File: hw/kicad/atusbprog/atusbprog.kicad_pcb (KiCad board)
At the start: 2 copper layers, 26 parts, among them J1 SMH-110-02-L-D, J2 Conn_01x04, J3 Conn_01x08, J4 Conn_01x08, J5 Conn_01x08, SW1 SW_Push, SW2 SW_Push, U1 SN74HCT125, U2 AT89S52-24PU, Y1 24 MHz

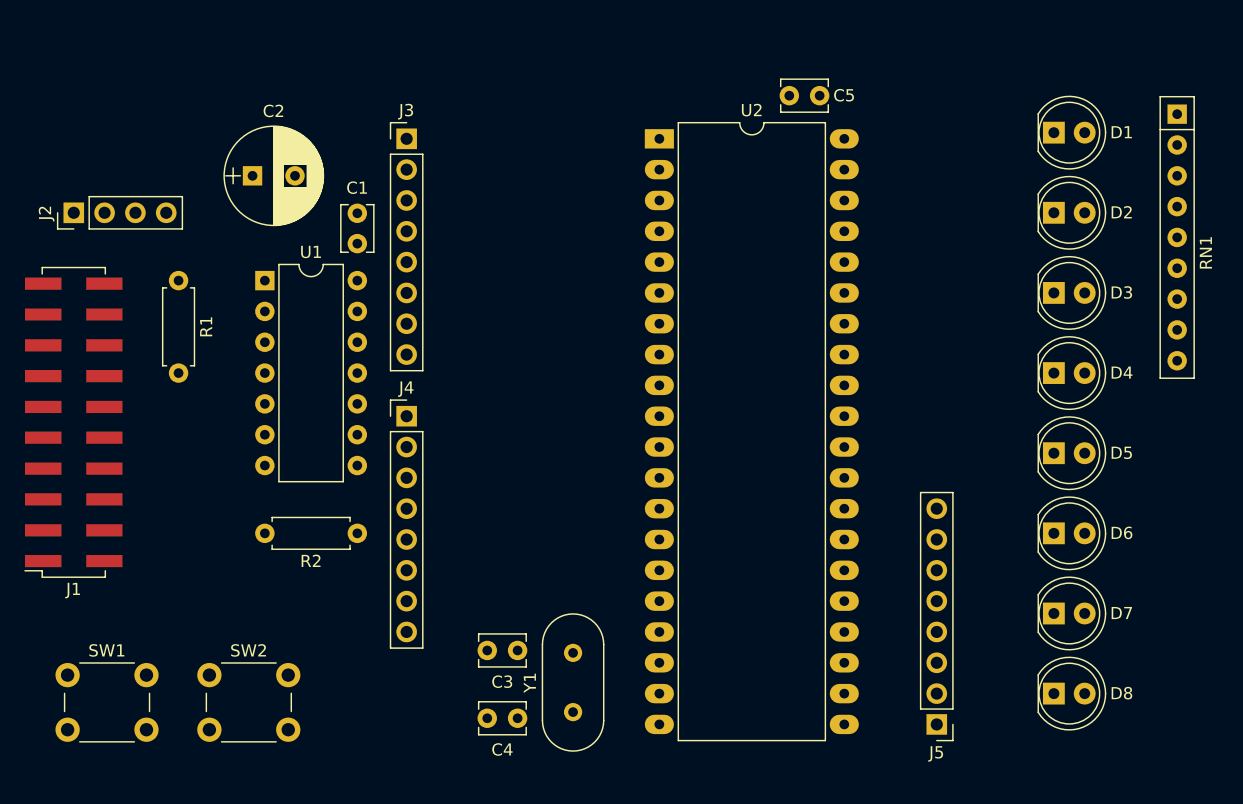
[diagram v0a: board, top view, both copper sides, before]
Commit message: Update to KiCAD 5.1.5, add silk marks
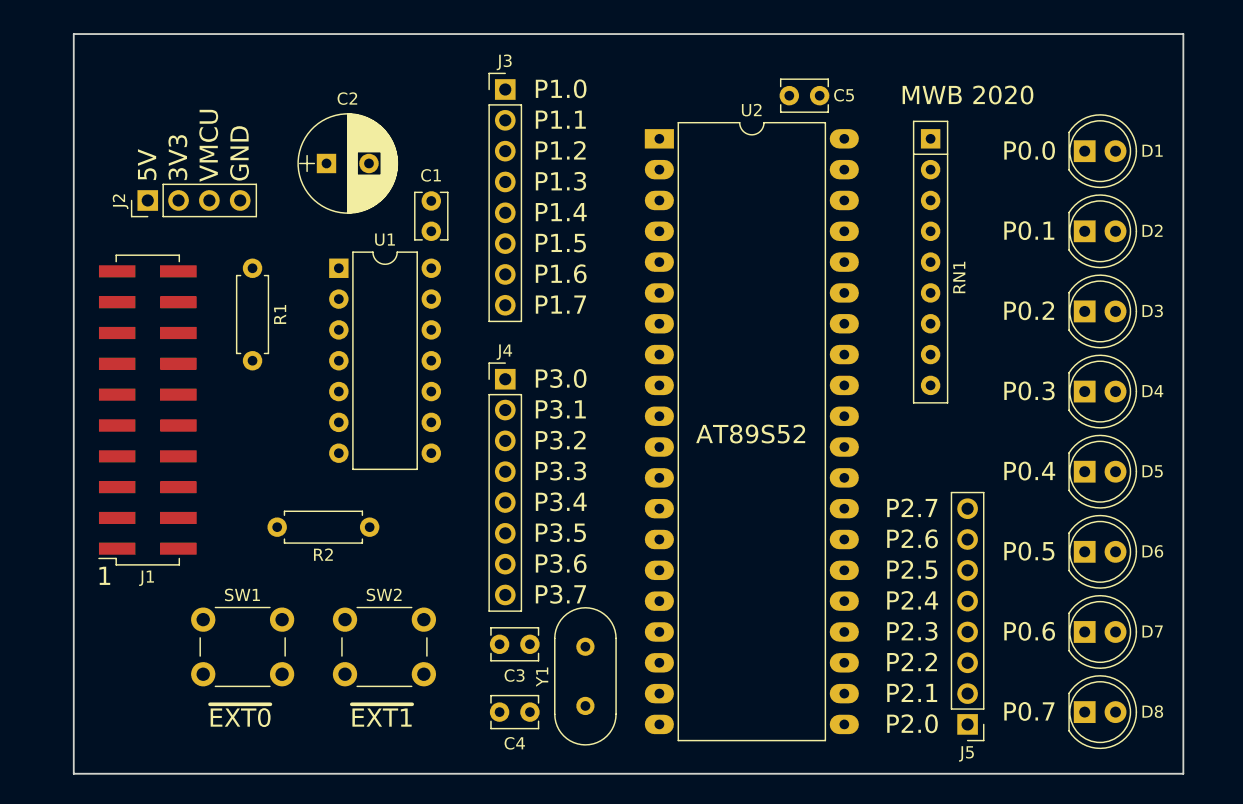
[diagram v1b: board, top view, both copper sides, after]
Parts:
- moved RN1 20.4 mm to (175.3, 74.7)
- moved SW1 12.1 mm to (115.3, 114.3)
- moved SW2 12.1 mm to (127.0, 114.3)
- moved J3 9.09 mm to (140.2, 70.6)
- moved J4 8.68 mm to (140.2, 94.5)
- moved C2 6.18 mm to (125.5, 76.7)
- moved J2 6.18 mm to (110.7, 79.8)
- moved U1 6.18 mm to (126.5, 85.3)
- moved C1 6.18 mm to (134.1, 82.3)
- moved J1 6.18 mm to (110.7, 97.0)
- moved R1 6.18 mm to (119.4, 85.3)
- moved D2 2.96 mm to (188.0, 82.3)
- moved D3 2.96 mm to (188.0, 88.9)
- moved D4 2.96 mm to (188.0, 95.5)
- moved D5 2.96 mm to (188.0, 102.1)
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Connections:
- J1 pad 2: +3V3 -> +VMCU
- J2 pad 3: +3V3 -> +VMCU
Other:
- board outline added: 91.4 x 61 mm
- board text added: "1"
- board text added: "3V3"
- board text added: "5V"
- board text added: "AT89S52"
- board text added: "ATUSBPROG V1"
- board text added: "GND"
- board text added: "MWB 2020"
- board text added: "P0.0"
- board text added: "P0.1"
- board text added: "P0.2"
- board text added: "P0.3"
- board text added: "P0.4"
- board text added: "P0.5"
- board text added: "P0.6"
- board text added: "P0.7"
- board text added: "P1.0"
- board text added: "P1.1"
- board text added: "P1.2"
- board text added: "P1.3"
- board text added: "P1.4"
- board text added: "P1.5"
- board text added: "P1.6"
- board text added: "P1.7"
- board text added: "P2.0"
- board text added: "P2.1"
- board text added: "P2.2"
- board text added: "P2.3"
- board text added: "P2.4"
- board text added: "P2.5"
- board text added: "P2.6"
- board text added: "P2.7"
- board text added: "P3.0"
- board text added: "P3.1"
- board text added: "P3.2"
- board text added: "P3.3"
- board text added: "P3.4"
- board text added: "P3.5"
- board text added: "P3.6"
- board text added: "P3.7"
- board text added: "VMCU"
- board text added: "~EXT0"
- board text added: "~EXT1"

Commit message: Update PCB V1
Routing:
- net /BTN0: track 0.00 -> 52.6 mm
- net ATS_MISO: track 0.00 -> 48.5 mm, vias 0 -> 1
- net EFM_OE_N: track 0.00 -> 43.6 mm
- net /BTN1: track 0.00 -> 39.9 mm
- net Net-(D8-Pad1): track 0.00 -> 36.8 mm
- net ATS_SCK: track 0.00 -> 33.7 mm
- net +VMCU: track 0.00 -> 33.5 mm, vias 0 -> 1
- net ATS_MOSI: track 0.00 -> 33.5 mm
- net Net-(D8-Pad2): track 0.00 -> 33.2 mm
- net EFM_MOSI: track 0.00 -> 32.0 mm, vias 0 -> 1
- net Net-(D7-Pad1): track 0.00 -> 31.3 mm
- net EFM_AUX: track 0.00 -> 30.2 mm, vias 0 -> 2
- net EFM_RST: track 0.00 -> 29.4 mm
- net Net-(D7-Pad2): track 0.00 -> 29.2 mm
- net Net-(D6-Pad1): track 0.00 -> 27.7 mm
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- added copper zone on B.Cu, net +5V
- added copper zone on F.Cu, net GND
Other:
- net class Default: clearance 0.2 -> 0.1524
- rule pad_to_mask_clearance: 0.2 -> 0.0508
- rule trace_clearance: 0.2 -> 0.1524
- rule trace_min: 0.2 -> 0.1524
- rule via_min_drill: 0.3 -> 0.254
- rule via_min_size: 0.4 -> 0.254

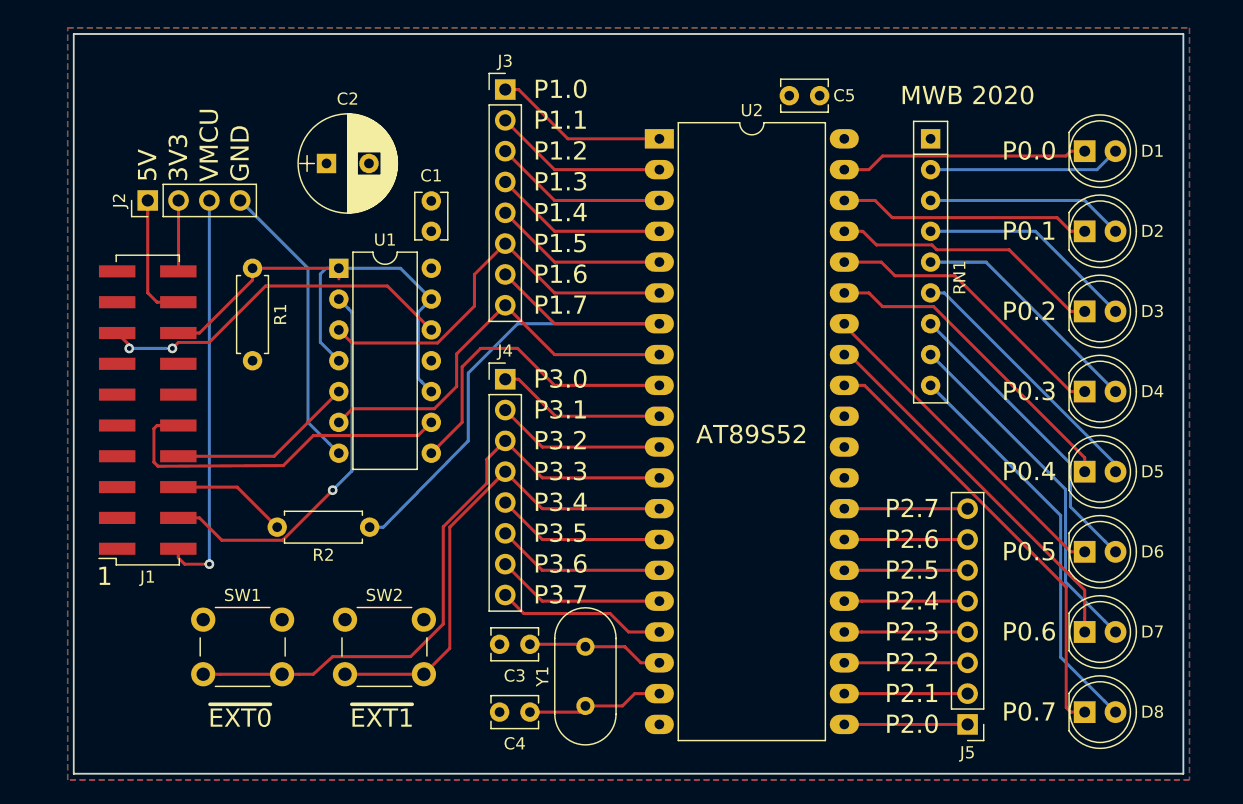
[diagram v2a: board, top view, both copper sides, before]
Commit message: Add power LEDs
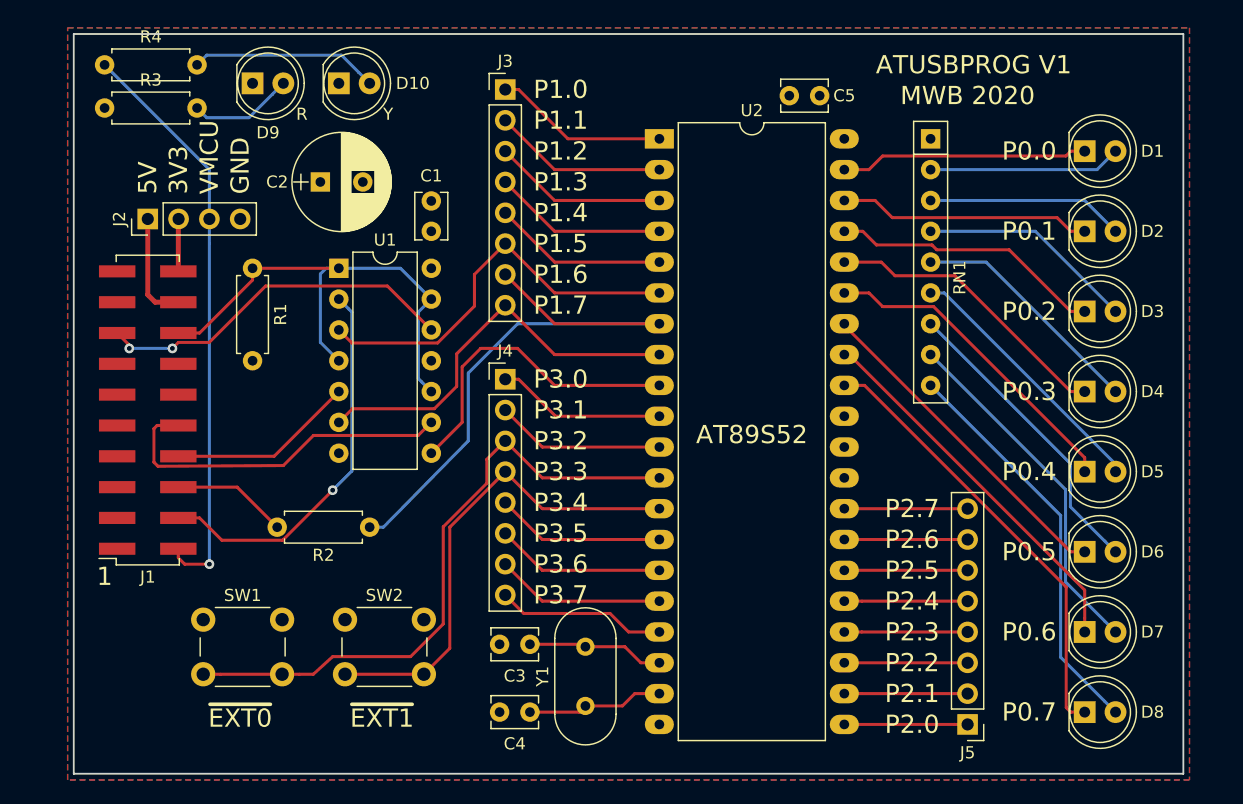
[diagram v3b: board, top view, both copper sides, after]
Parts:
- added D10: LTL2R3KYD-EM, LEDs:LED_D5.0mm, F.Cu at (126.5, 70.1)
- added D9: LTL2R3KRD-EM, LEDs:LED_D5.0mm, F.Cu at (119.4, 70.1)
- added R3: 1.2k, Resistors_THT:R_Axial_DIN0207_L6.3mm_D2.5mm_P7.62mm_Horizontal, F.Cu at (107.2, 72.1)
- added R4: 1.2k, Resistors_THT:R_Axial_DIN0207_L6.3mm_D2.5mm_P7.62mm_Horizontal, F.Cu at (107.2, 68.6)
- moved C2 1.61 mm to (125.0, 78.2)
- moved J2 1.52 mm to (110.7, 81.3)
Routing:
- net GND: track 24.2 -> 0.00 mm
- net Net-(D10-Pad2): track 0.00 -> 15.5 mm
- net +VMCU: track 33.5 -> 48.3 mm
- net Net-(D9-Pad2): track 0.00 -> 8.62 mm
- net +3V3: track 5.85 -> 4.35 mm
- net +5V: track 10.8 -> 9.38 mm
- net EFM_OE_N: track 43.6 -> 42.7 mm
- net ATS_MISO: vias 1 -> 0
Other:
- board text added: "R"
- board text added: "Y"
